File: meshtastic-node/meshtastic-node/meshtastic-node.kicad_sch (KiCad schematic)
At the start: 111 parts, among them IC1 CH224K, IC2 CN3791, IC3 SKY65313-21, IC4 TPS2121RUXT, IC5 Wio-WM1110, IC7 TPS2121RUXT, J1 USB_C_Receptacle_USB2.0, J2 Conn_01x05_Socket, J3 Conn_Coaxial_Small, J4 Conn_01x02_Socket, J5 Conn_01x02_Socket, J6 Conn_ARM_JTAG_SWD_10, Q1 PMOS, Q2 PMOS, SW2 SW_Push, SW3 SW_DPDT_x2, U1 TPS565208, U2 TPS61222DCK, U3 TPS61222DCK, U4 BME280, U5 INA3221

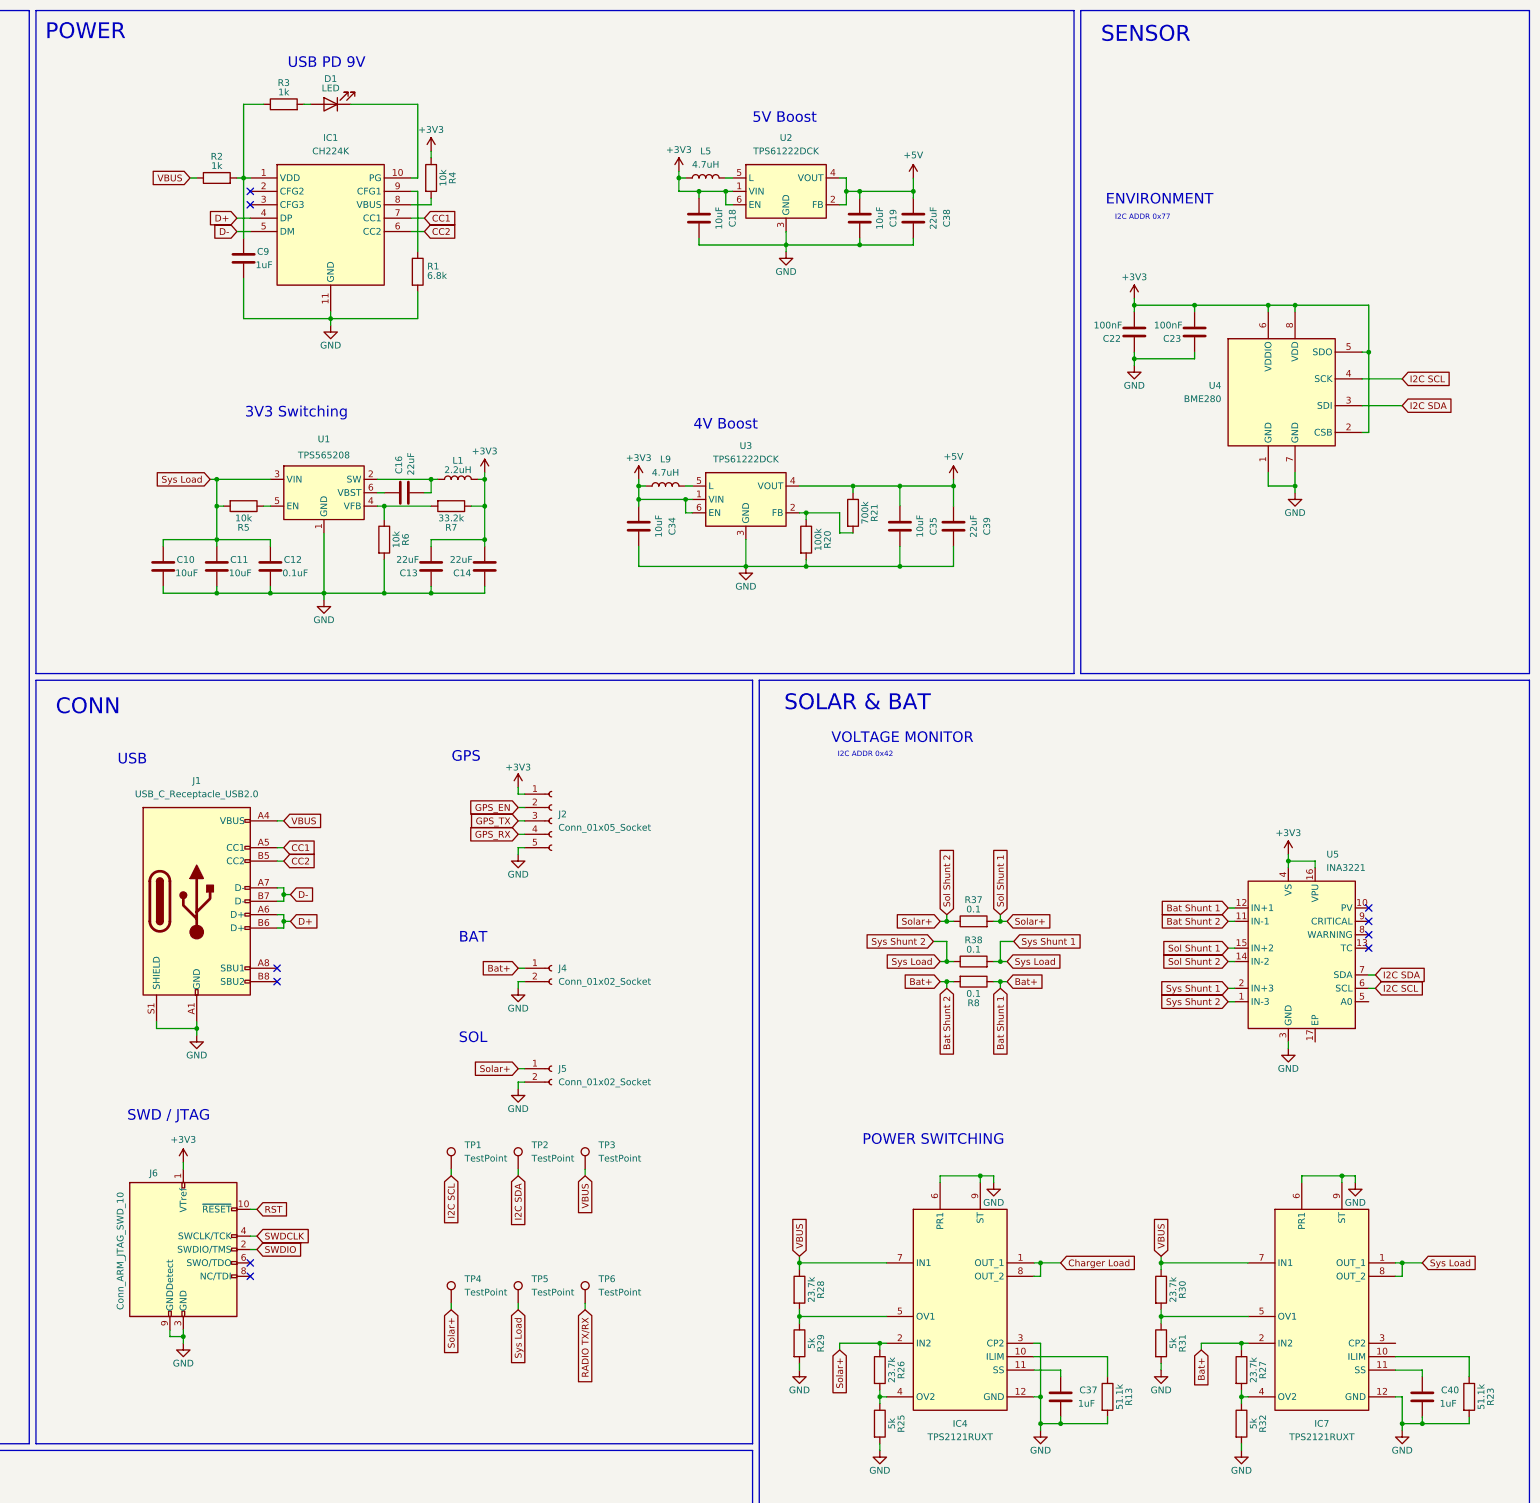
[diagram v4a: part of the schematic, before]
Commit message: Most component selection
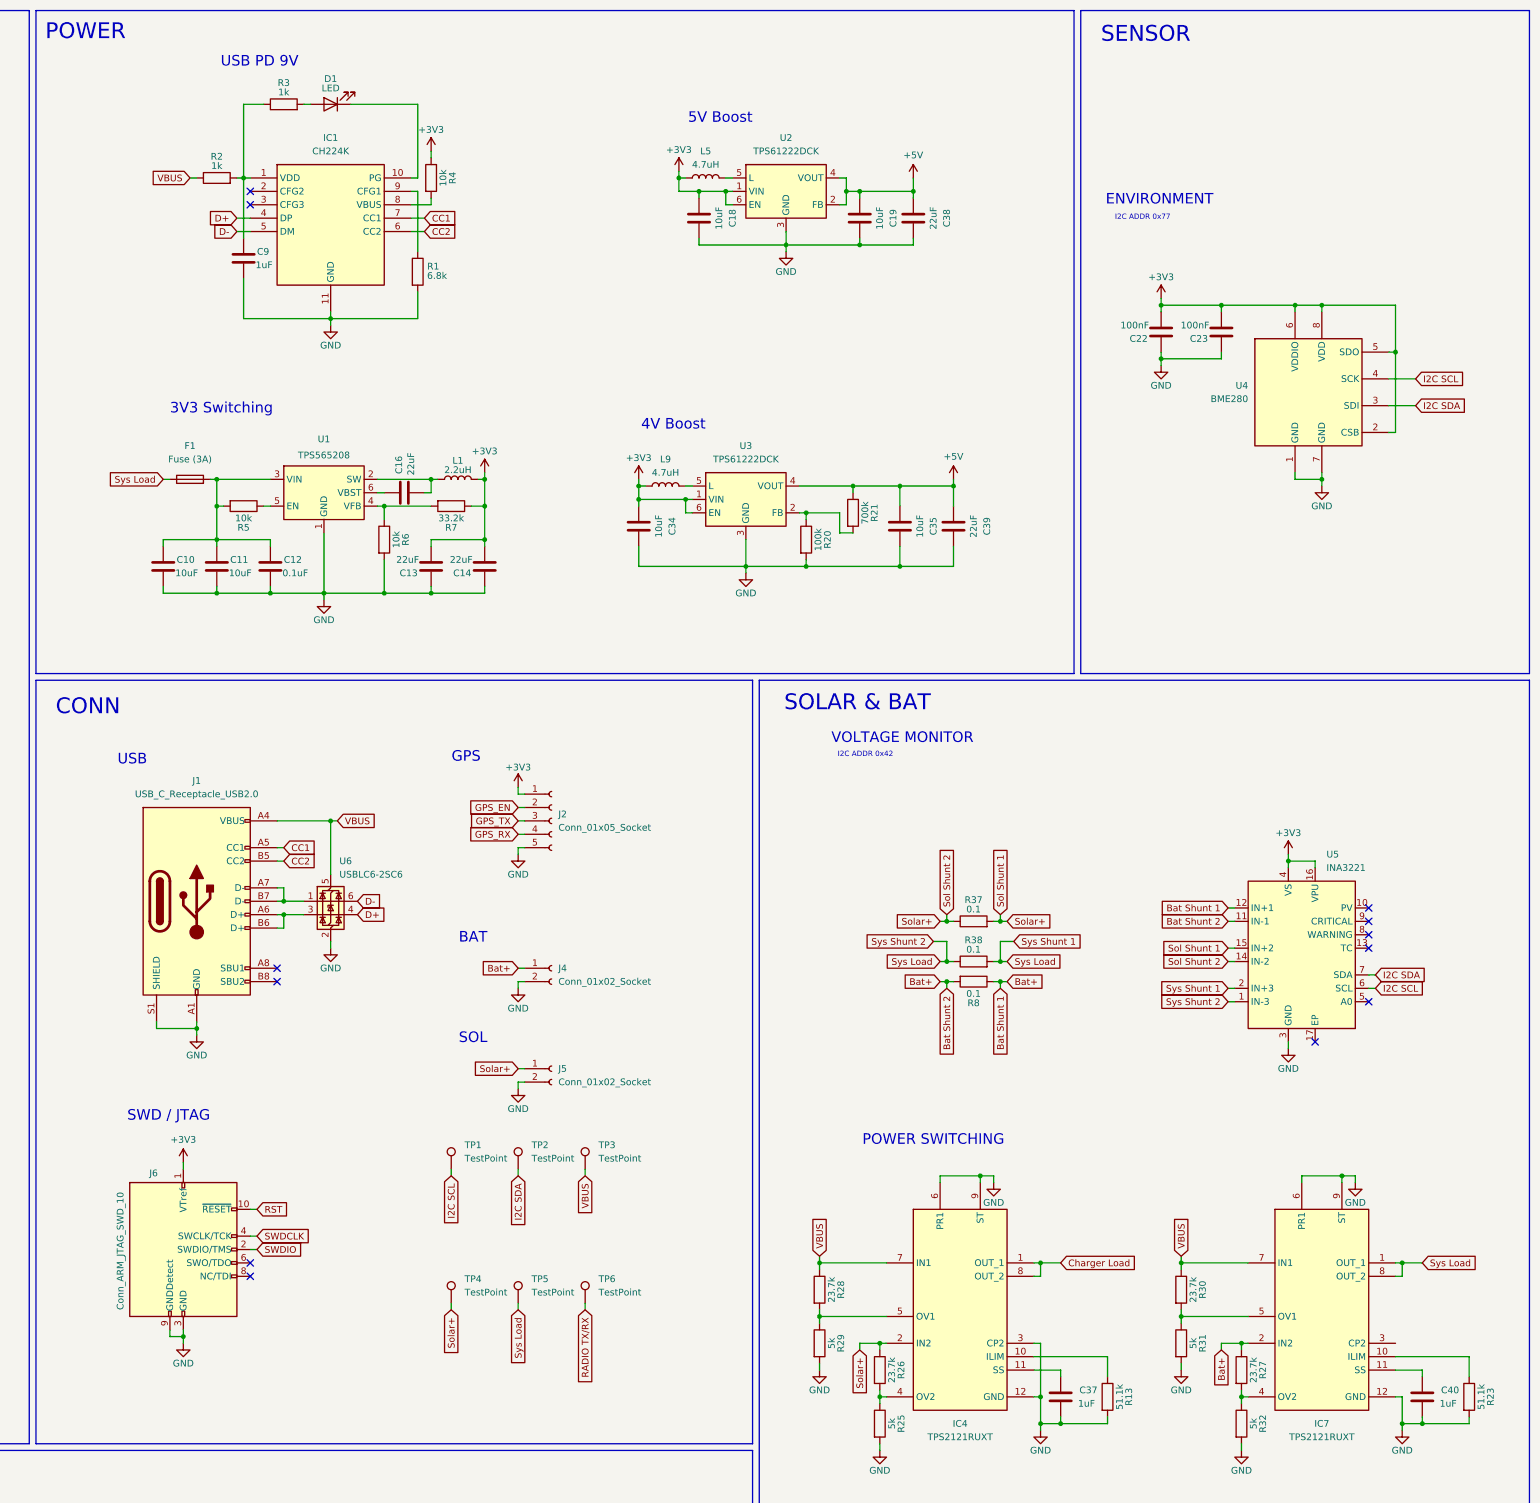
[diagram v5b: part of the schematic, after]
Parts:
- added F1: Fuse (3A), Fuse:Fuse_0603_1608Metric_Pad1.05x0.95mm_HandSolder, symbol Device:Fuse
- added U6: USBLC6-2SC6, Package_TO_SOT_SMD:SOT-23-6, symbol Power_Protection:USBLC6-2SC6
- C17, C24: footprint (none) -> Capacitor_SMD:CP_Elec_4x5.4
- D6: footprint (none) -> Diode_SMD:D_SMA
- IC1: footprint SOP100P600X180-11N -> meshtastic:SOP100P600X180-11N
- IC2: footprint SOP100P600X175-10N -> meshtastic:SOP100P600X175-10N
- IC3: footprint SKY6531321 -> meshtastic:SKY6531321
- IC4, IC7: footprint TPS2121RUXT -> TPS:TPS2121RUXT
- IC5: footprint WioWM1110 -> meshtastic:WioWM1110
- S1: footprint SOT95P280X145-6N -> meshtastic:SOT95P280X145-6N
- SW2: footprint (none) -> Button_Switch_SMD:SW_Push_1P1T_XKB_TS-1187A
- SW3: footprint (none) -> meshtastic:SS3235SL3
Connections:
- net D+: now also U6.4 (I/O2); no longer J1.A6 (D+), J1.B6 (D+)
- net D-: now also U6.6 (I/O1); no longer J1.A7 (D-), J1.B7 (D-)
- net GND: now also U6.2 (GND)
- net Sys Load: now also F1.1; no longer C10.1, C11.1, C12.1, R5.2, U1.3 (VIN)
- net VBUS: now also U6.5 (VBUS)
- new net: C10.1, C11.1, C12.1, F1.2, R5.2, U1.3 (VIN)
- new net: J1.A7 (D-), J1.B7 (D-), U6.1 (I/O1)
- new net: J1.A6 (D+), J1.B6 (D+), U6.3 (I/O2)
- no-connect marks 47 -> 49
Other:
- moved on the sheet: C22, C23, R28, R29, R30, R31, U4

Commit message: better part selection
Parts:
- IC1: LCSC (none) -> C970725
- IC2: LCSC (none) -> C154992
- IC3: LCSC (none) -> C5144140
- IC4, IC7: LCSC (none) -> C2156025
- L1: footprint Inductor_SMD_Wurth:L_Wurth_WE-LQSH-4020 -> Inductor_SMD:L_SXN_SMDRI124; LCSC (none) -> C2929497
- S1: LCSC (none) -> C579555
- SW2: LCSC (none) -> C42420254
- SW3: LCSC (none) -> C381098
- U1: LCSC (none) -> C2650336
- U2, U3: LCSC (none) -> C116461
- U4: LCSC (none) -> C92489
- U5: LCSC (none) -> C181255
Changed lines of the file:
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@@
 			)
 		)
+		(property "LCSC" "C381098"
+			(at 43.18 317.5 0)
+			(effects
+				(font
+					(size 1.27 1.27)
+				)
+				(hide yes)
+			)
+		)
+		(property "Field6" ""
+			(at 43.18 317.5 0)
+			(effects
+				(font
+					(size 1.27 1.27)
+				)
+				(hide yes)
+			)
+		)
 		(pin "3"
 		)
@@
 			)
 		)
+		(property "LCSC" "C579555"
+			(at 149.86 323.85 0)
+			(effects
+				(font
+					(size 1.27 1.27)
+				)
+				(hide yes)
+			)
+		)
 		(pin "3"
 		)
@@
 			)
 		)
+		(property "LCSC" "C92489"
+			(at 391.16 85.09 0)
+			(effects
+				(font
+					(size 1.27 1.27)
+				)
+				(hide yes)
+			)
+		)
 		(pin "1"
 		)
@@
 			)
 		)
+		(property "LCSC" "C2156025"
+			(at 379.73 250.19 0)
+			(effects
+				(font
+					(size 1.27 1.27)
+				)
+				(hide yes)
+			)
+		)
 		(pin "10"
 		)
@@
 			)
 		)
+		(property "LCSC" "C116461 "
+			(at 284.48 105.41 0)
+			(effects
+				(font
+					(size 1.27 1.27)
+				)
+				(hide yes)
+			)
+		)
 		(pin "1"
 		)
@@
 			)
 		)
+		(property "LCSC" "C154992"
+			(at 336.55 341.63 0)
+			(effects
+				(font
+					(size 1.27 1.27)
+				)
+				(hide yes)
+			)
+		)
 		(pin "1"
 		)
@@
 			)
 		)
+		(property "LCSC" "C2156025"
+			(at 311.15 250.19 0)
+			(effects
+				(font
+					(size 1.27 1.27)
+				)
+				(hide yes)
+			)
+		)
 		(pin "10"
 		)
@@
 			)
 		)
+		(property "LCSC" "C42420254"
+			(at 74.93 270.51 0)
+			(effects
+				(font
+					(size 1.27 1.27)
+				)
+				(hide yes)
+			)
+		)
+		(property "Field6" ""
+			(at 74.93 270.51 0)
+			(effects
+				(font
+					(size 1.27 1.27)
+				)
+				(hide yes)
+			)
+		)
 		(pin "2"
 		)
@@
 			)
 		)
-		(property "Footprint" "Inductor_SMD_Wurth:L_Wurth_WE-LQSH-4020"
+		(property "Footprint" "Inductor_SMD:L_SXN_SMDRI124"
 			(at 229.87 101.6 0)
 			(effects
@@
 			)
 		)
+		(property "LCSC" "C2929497"
+			(at 229.87 101.6 90)
+			(effects
+				(font
+					(size 1.27 1.27)
+				)
+				(hide yes)
+			)
+		)
 		(pin "1"
 		)
@@
 			)
 		)
+		(property "LCSC" "C116461"
+			(at 292.1 46.99 0)
+			(effects
+				(font
+					(size 1.27 1.27)
+				)
+				(hide yes)
+			)
+		)
 		(pin "1"
 		)
@@
 			)
 		)
+		(property "LCSC" "C181255"
+			(at 389.89 193.04 0)
+			(effects
+				(font
+					(size 1.27 1.27)
+				)
+				(hide yes)
+			)
+		)
+		(property "Field6" ""
+			(at 389.89 193.04 0)
+			(effects
+				(font
+					(size 1.27 1.27)
+				)
+				(hide yes)
+			)
+		)
 		(pin "7"
 		)
@@
 			)
 		)
+		(property "LCSC" "C5144140"
+			(at 240.03 373.38 0)
+			(effects
+				(font
+					(size 1.27 1.27)
+				)
+				(hide yes)
+			)
+		)
 		(pin "9"
 		)
@@
 			)
 		)
+		(property "LCSC" "C970725"
+			(at 190.5 44.45 0)
+			(effects
+				(font
+					(size 1.27 1.27)
+				)
+				(hide yes)
+			)
+		)
 		(pin "10"
 		)
@@
 			(at 204.47 104.14 0)
 			(effects
+				(font
+					(size 1.27 1.27)
+				)
+				(hide yes)
+			)
+		)
+		(property "LCSC" "C2650336"
+			(at 204.47 104.14 0)
+			(effects

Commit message: routing
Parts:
- removed AE1: Antenna_Shield, symbol Device:Antenna_Shield
- added J7: Conn_Coaxial_Small, Connector_Coaxial:SMA_Molex_73251-1153_EdgeMount_Horizontal, symbol Connector:Conn_Coaxial_Small
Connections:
- net +3V3: no longer SW3.2 (B)
- net +4V: now also SW3.2 (B); no longer C25.1, C26.1, C27.1, C28.1, IC3.23 (VDD2), IC3.24 (VCC_TX1), IC3.25 (VCC_TX2), IC3.26 (VCC_TX3)
- net GND: now also J7.2 (Ext)
- net USE_ANT_2: now also C25.1, C26.1, C27.1, C28.1, IC3.23 (VDD2), IC3.24 (VCC_TX1), IC3.25 (VCC_TX2), IC3.26 (VCC_TX3)
- net at S1.1 (RF2): now also J7.1 (In)
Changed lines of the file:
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@@
 	(wire
 		(pts
-			(xy 163.83 322.58) (xy 163.83 323.85)
-		)
-		(stroke
-			(width 0)
-			(type default)
-		)
-	)
-	(wire
-		(pts
 			(xy 60.96 194.31) (xy 62.23 194.31)
 		)
@@
 	(wire
 		(pts
-			(xy 161.29 323.85) (xy 161.29 322.58)
-		)
-		(stroke
-			(width 0)
-			(type default)
-		)
-	)
-	(wire
-		(pts
 			(xy 60.96 146.05) (xy 62.23 146.05)
 		)
@@
 	(wire
 		(pts
+			(xy 163.83 325.12) (xy 163.83 323.85)
+		)
+		(stroke
+			(width 0)
+			(type default)
+		)
+	)
+	(wire
+		(pts
 			(xy 340.36 265.43) (xy 340.36 275.59)
 		)
@@
 	(wire
 		(pts
-			(xy 149.86 323.85) (xy 161.29 323.85)
+			(xy 149.86 323.85) (xy 158.75 323.85)
 		)
 		(stroke
@@
 		)
 	)
+	(global_label "USE_ANT_2"
+		(shape input)
+		(at 154.94 364.49 90)
+		(fields_autoplaced yes)
+		(effects
+			(font
+				(size 1.27 1.27)
+			)
+			(justify left)
+		)
+		(property "Intersheetrefs" "${INTERSHEET_REFS}"
+			(at 154.94 351.2844 90)
+			(effects
+				(font
+					(size 1.27 1.27)
+				)
+				(justify left)
+				(hide yes)
+			)
+		)
+	)
 	(global_label "I2C SCL"
 		(shape input)
@@
 	)
 	(symbol
+		(lib_id "Connector:Conn_Coaxial_Small")
+		(at 161.29 323.85 0)
+		(unit 1)
+		(exclude_from_sim no)
+		(in_bom yes)
+		(on_board yes)
+		(dnp no)
+		(fields_autoplaced yes)
+		(property "Reference" "J7"
+			(at 160.7704 317.5 0)
+			(effects
+				(font
+					(size 1.27 1.27)
+				)
+			)
+		)
+		(property "Value" "Conn_Coaxial_Small"
+			(at 160.7704 320.04 0)
+			(effects
+				(font
+					(size 1.27 1.27)
+				)
+			)
+		)
+		(property "Footprint" "Connector_Coaxial:SMA_Molex_73251-1153_EdgeMount_Horizontal"
+			(at 161.29 323.85 0)
+			(effects
+				(font
+					(size 1.27 1.27)
+				)
+				(hide yes)
+			)
+		)
+		(property "Datasheet" "~"
+			(at 161.29 323.85 0)
+			(effects
+				(font
+					(size 1.27 1.27)
+				)
+				(hide yes)
+			)
+		)
+		(property "Description" "small coaxial connector (BNC, SMA, SMB, SMC, Cinch/RCA, LEMO, ...)"
+			(at 161.29 323.85 0)
+			(effects
+				(font
+					(size 1.27 1.27)
+				)
+				(hide yes)
+			)
+		)
+		(pin "2"
+		)
+		(pin "1"
+		)
+		(instances
+			(project "meshtastic-node"
+				(path "/78793cd8-747c-4577-866f-2f46519ee26a"
+					(reference "J7")
+					(unit 1)
+				)
+			)
+		)
+	)
+	(symbol
 		(lib_id "Device:C")
 		(at 167.64 370.84 0)
@@
 	(symbol
 		(lib_id "power:+4V")
-		(at 154.94 364.49 0)
+		(at 33.02 316.23 0)
 		(unit 1)
 		(exclude_from_sim no)
@@
 		(dnp no)
 		(property "Reference" "#PWR014"
-			(at 154.94 368.3 0)
+			(at 33.02 320.04 0)
 			(effects
 				(font
@@
 		)
 		(property "Value" "+4V"
-			(at 154.178 359.918 0)
+			(at 32.258 311.658 0)
 			(effects
 				(font
@@
 		)
 		(property "Footprint" ""
-			(at 154.94 364.49 0)
+			(at 33.02 316.23 0)
 			(effects
 				(font
@@
 		)
 		(property "Datasheet" ""
-			(at 154.94 364.49 0)
+			(at 33.02 316.23 0)
 			(effects
 				(font
@@
 		)
 		(property "Description" "Power symbol creates a global label with name \"+4V\""
-			(at 154.94 364.49 0)
+			(at 33.02 316.23 0)
 			(effects
 				(font
@@
 		)
 		(instances
-			(project ""
+			(project "meshtastic-node"
 				(path "/78793cd8-747c-4577-866f-2f46519ee26a"
 					(reference "#PWR014")
@@
 	)
 	(symbol
-		(lib_id "Device:Antenna_Shield")
-		(at 161.29 317.5 0)
-		(unit 1)
-		(exclude_from_sim no)
-		(in_bom yes)
-		(on_board yes)
-		(dnp no)
-		(fields_autoplaced yes)
-		(property "Reference" "AE1"
-			(at 165.1 315.5949 0)
-			(effects
-				(font
-					(size 1.27 1.27)
-				)
-				(justify left)
-			)
-		)
-		(property "Value" "Antenna_Shield"
-			(at 165.1 318.1349 0)
-			(effects
-				(font
-					(size 1.27 1.27)
-				)
-				(justify left)
-			)
-		)
-		(property "Footprint" ""
-			(at 161.29 314.96 0)
-			(effects
-				(font
-					(size 1.27 1.27)
-				)
-				(hide yes)
-			)
-		)
-		(property "Datasheet" "~"
-			(at 161.29 314.96 0)
-			(effects
-				(font
-					(size 1.27 1.27)
-				)
-				(hide yes)
-			)
-		)
-		(property "Description" "Antenna with extra pin for shielding"
-			(at 161.29 317.5 0)
-			(effects
-				(font
-					(size 1.27 1.27)
-				)
-				(hide yes)
-			)
-		)
-		(pin "2"
-		)
-		(pin "1"
-		)
-		(instances
-			(project ""
-				(path "/78793cd8-747c-4577-866f-2f46519ee26a"
-					(reference "AE1")
-					(unit 1)
-				)
-			)
-		)
-	)
-	(symbol
 		(lib_id "power:GND")
 		(at 387.35 209.55 0)
@@
 	(symbol
 		(lib_id "power:GND")
-		(at 163.83 323.85 0)
+		(at 163.83 325.12 0)
 		(unit 1)
 		(exclude_from_sim no)
@@
 		(dnp no)
 		(property "Reference" "#PWR018"
-			(at 163.83 330.2 0)
+			(at 163.83 331.47 0)
 			(effects
 				(font
@@
 		)
 		(property "Value" "GND"
-			(at 163.83 327.66 0)
+			(at 163.83 328.93 0)
 			(effects
 				(font
@@
 		)
 		(property "Footprint" ""
-			(at 163.83 323.85 0)
+			(at 163.83 325.12 0)
 			(effects
 				(font
@@
 		)
 		(property "Datasheet" ""
-			(at 163.83 323.85 0)
+			(at 163.83 325.12 0)
 			(effects
 				(font
@@
 		)
 		(property "Description" ""
-			(at 163.83 323.85 0)
+			(at 163.83 325.12 0)
 			(effects
 				(font
@@
 					(unit 1)
 				)
-			)
-		)
-	)
-	(symbol
-		(lib_id "power:+3V3")
-		(at 33.02 316.23 0)
-		(unit 1)
-		(exclude_from_sim no)
-		(in_bom yes)
-		(on_board yes)
-		(dnp no)
-		(property "Reference" "#PWR072"
-			(at 33.02 320.04 0)
-			(effects
-				(font
-					(size 1.27 1.27)
-				)
-				(hide yes)
-			)
-		)
-		(property "Value" "+3V3"
-			(at 33.02 311.912 0)
-			(effects
-				(font
-					(size 1.27 1.27)
-				)
-			)
-		)
-		(property "Footprint" ""
-			(at 33.02 316.23 0)
-			(effects
-				(font
-					(size 1.27 1.27)
-				)
-				(hide yes)
-			)
-		)
-		(property "Datasheet" ""
-			(at 33.02 316.23 0)
-			(effects
-				(font
-					(size 1.27 1.27)
-				)
-				(hide yes)
-			)
-		)
-		(property "Description" ""
-			(at 33.02 316.23 0)
-			(effects
-				(font
-					(size 1.27 1.27)
-				)
-				(hide yes)
-			)
-		)
-		(pin "1"
-		)
-		(instances
-			(project "meshtastic-node"
-				(path "/78793cd8-747c-4577-866f-2f46519ee26a"
-					(reference "#PWR072")
-					(unit 1)
-				)
